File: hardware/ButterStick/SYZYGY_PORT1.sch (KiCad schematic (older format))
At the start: 2 parts, among them U3 ECP5U25

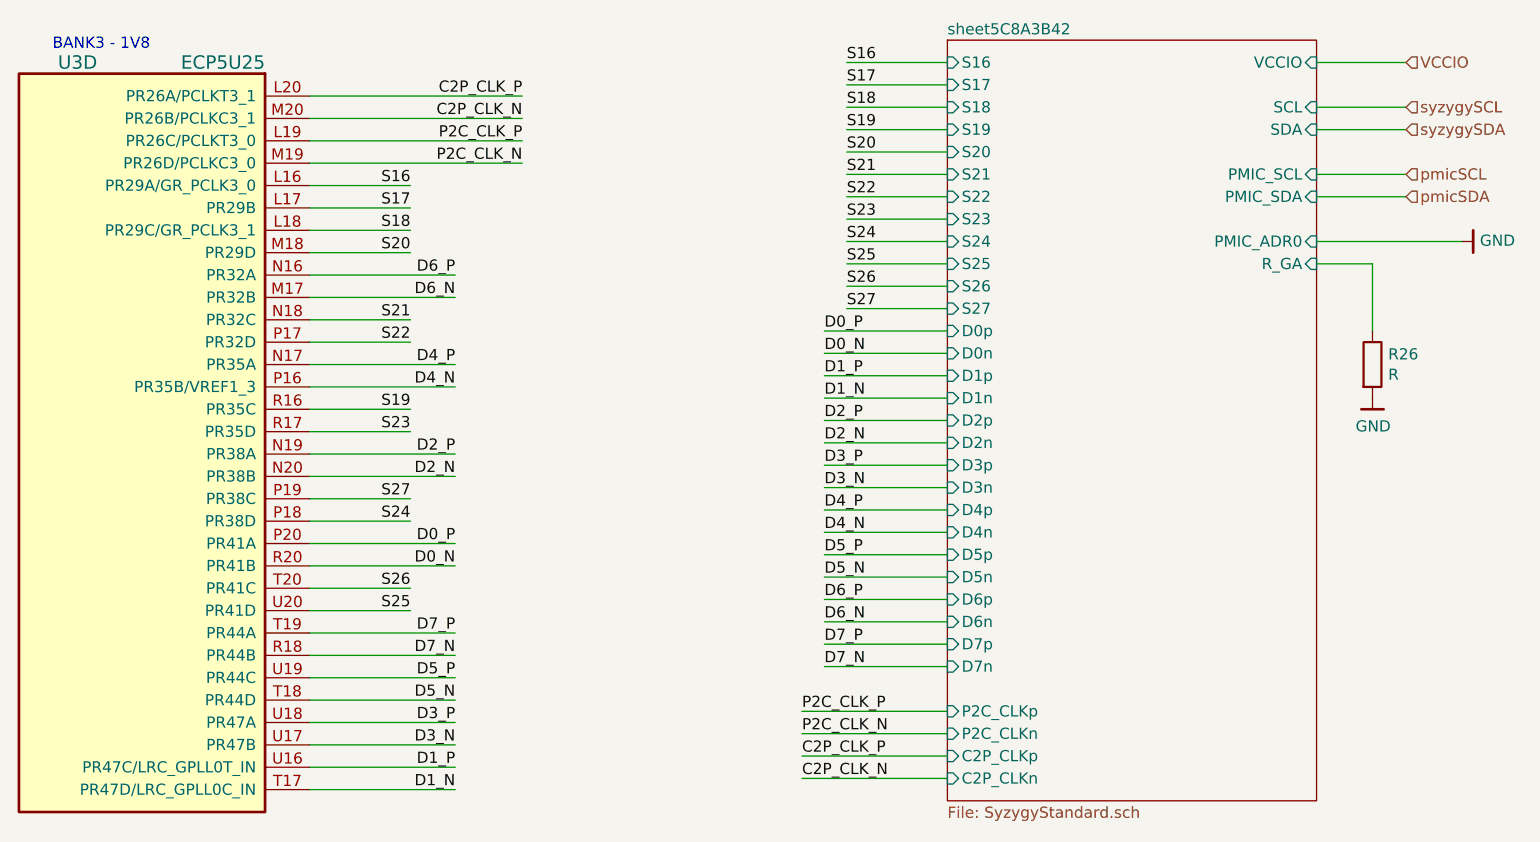
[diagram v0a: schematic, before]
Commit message: Routed all SYZYGY ports. Placed decoupling caps etc.
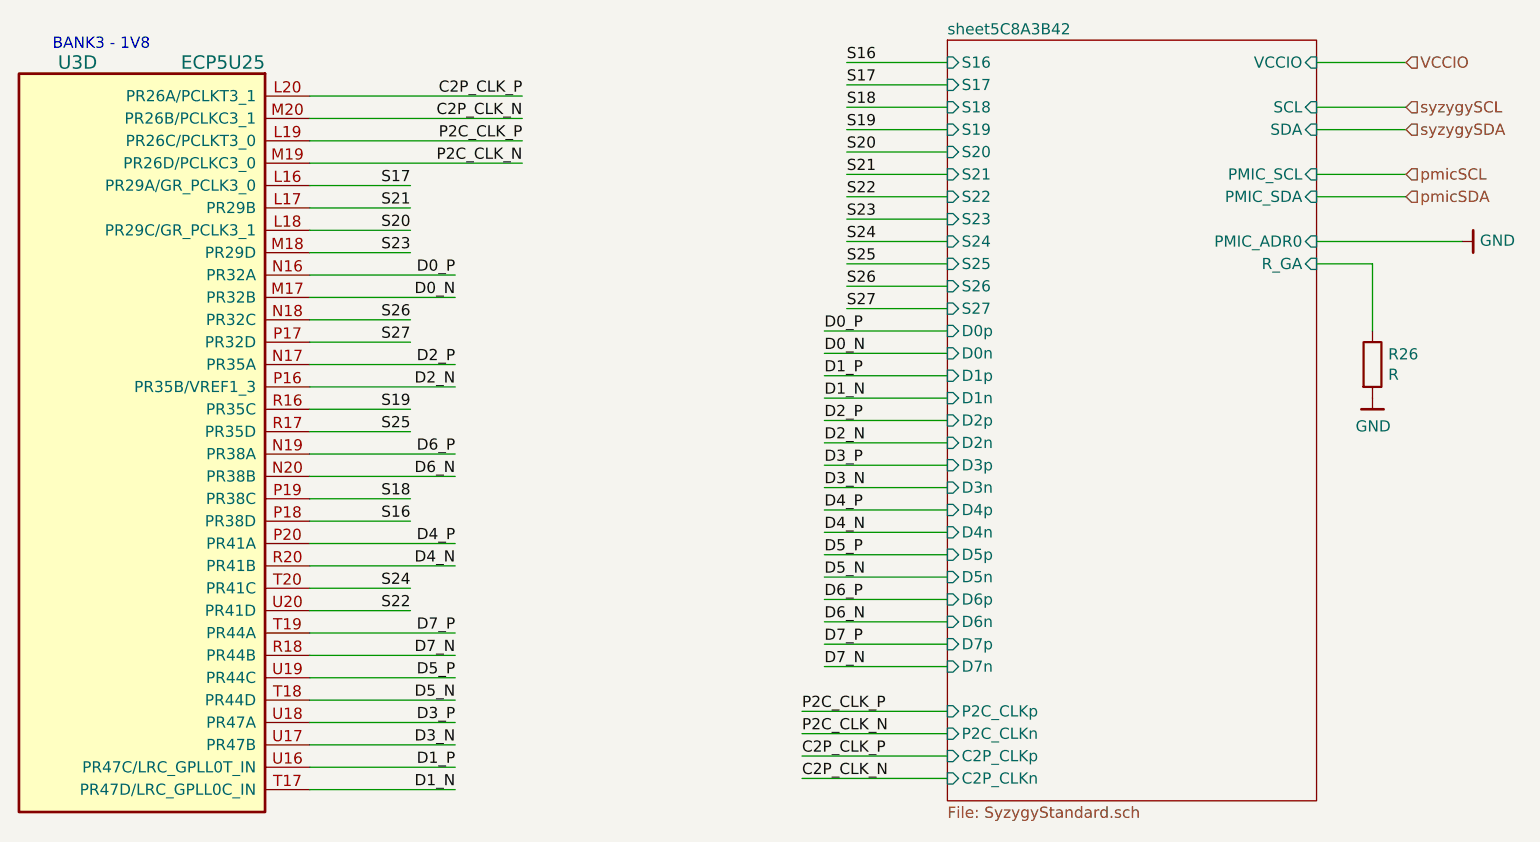
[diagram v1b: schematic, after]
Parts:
- R26: footprint (none) -> pkl_dipol:R_0402
- U3: footprint (none) -> gkl_housings_bga:caBGA_381_17x17
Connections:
- net D0_N: now also U3.M17 (PR32B); no longer U3.R20 (PR41B)
- net D0_P: now also U3.N16 (PR32A); no longer U3.P20 (PR41A)
- net D2_N: now also U3.P16 (PR35B/VREF1_3); no longer U3.N20 (PR38B)
- net D2_P: now also U3.N17 (PR35A); no longer U3.N19 (PR38A)
- net D4_N: now also U3.R20 (PR41B); no longer U3.P16 (PR35B/VREF1_3)
- net D4_P: now also U3.P20 (PR41A); no longer U3.N17 (PR35A)
- net D6_N: now also U3.N20 (PR38B); no longer U3.M17 (PR32B)
- net D6_P: now also U3.N19 (PR38A); no longer U3.N16 (PR32A)
- net S16: now also U3.P18 (PR38D); no longer U3.L16 (PR29A/GR_PCLK3_0)
- net S17: now also U3.L16 (PR29A/GR_PCLK3_0); no longer U3.L17 (PR29B)
- net S18: now also U3.P19 (PR38C); no longer U3.L18 (PR29C/GR_PCLK3_1)
- net S20: now also U3.L18 (PR29C/GR_PCLK3_1); no longer U3.M18 (PR29D)
- net S21: now also U3.L17 (PR29B); no longer U3.N18 (PR32C)
- net S22: now also U3.U20 (PR41D); no longer U3.P17 (PR32D)
- net S23: now also U3.M18 (PR29D); no longer U3.R17 (PR35D)
- net S24: now also U3.T20 (PR41C); no longer U3.P18 (PR38D)
- net S25: now also U3.R17 (PR35D); no longer U3.U20 (PR41D)
- net S26: now also U3.N18 (PR32C); no longer U3.T20 (PR41C)
- net S27: now also U3.P17 (PR32D); no longer U3.P19 (PR38C)
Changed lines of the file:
@@
 $Descr A4 11693 8268
 encoding utf-8
-Sheet 10 13
+Sheet 10 14
 Title ""
 Date ""
@@
 F 0 "U3" H 4600 2600 60  0000 L CNN
 F 1 "ECP5U25" H 3850 2600 60  0000 L CNN
-F 2 "" H 3650 2450 50  0001 C CNN
+F 2 "gkl_housings_bga:caBGA_381_17x17" H 3650 2450 50  0001 C CNN
 F 3 "" H 3650 2450 50  0001 C CNN
 F 4 " 220-2052-ND " H -200 -1950 50  0001 C CNN "SN-DK"
@@
 C2P_CLK_N
 Wire Wire Line
+	3650 4350 4100 4350
+Wire Wire Line
 	3650 2850 4100 2850
 Wire Wire Line
+	3650 4250 4100 4250
+Wire Wire Line
+	3650 3850 4100 3850
+Wire Wire Line
+	3650 3050 4100 3050
+Wire Wire Line
 	3650 2950 4100 2950
 Wire Wire Line
-	3650 3050 4100 3050
-Wire Wire Line
-	3650 3850 4100 3850
+	3650 4750 4100 4750
 Wire Wire Line
 	3650 3150 4100 3150
 Wire Wire Line
+	3650 4650 4100 4650
+Wire Wire Line
+	3650 3950 4100 3950
+Wire Wire Line
 	3650 3450 4100 3450
 Wire Wire Line
 	3650 3550 4100 3550
 Wire Wire Line
-	3650 3950 4100 3950
-Wire Wire Line
-	3650 4350 4100 4350
-Wire Wire Line
-	3650 4750 4100 4750
-Wire Wire Line
-	3650 4650 4100 4650
-Wire Wire Line
-	3650 4250 4100 4250
+	3650 3250 4300 3250
+Wire Wire Line
+	3650 3350 4300 3350
+Wire Wire Line
+	3650 5450 4300 5450
+Wire Wire Line
+	3650 5550 4300 5550
+Wire Wire Line
+	3650 3650 4300 3650
+Wire Wire Line
+	3650 3750 4300 3750
+Wire Wire Line
+	3650 5250 4300 5250
+Wire Wire Line
+	3650 5350 4300 5350
 Wire Wire Line
 	3650 4450 4300 4450
@@
 	3650 4550 4300 4550
 Wire Wire Line
-	3650 5450 4300 5450
-Wire Wire Line
-	3650 5550 4300 5550
+	3650 5050 4300 5050
+Wire Wire Line
+	3650 5150 4300 5150
 Wire Wire Line
 	3650 4050 4300 4050
@@
 	3650 4150 4300 4150
 Wire Wire Line
-	3650 5250 4300 5250
-Wire Wire Line
-	3650 5350 4300 5350
-Wire Wire Line
-	3650 3650 4300 3650
-Wire Wire Line
-	3650 3750 4300 3750
-Wire Wire Line
-	3650 5050 4300 5050
-Wire Wire Line
-	3650 5150 4300 5150
-Wire Wire Line
-	3650 3250 4300 3250
-Wire Wire Line
-	3650 3350 4300 3350
-Wire Wire Line
 	3650 4850 4300 4850
 Wire Wire Line
@@
 Wire Wire Line
 	3650 2550 4600 2550
+Text Label 4100 4350 2    50   ~ 0
+S16
 Text Label 4100 2850 2    50   ~ 0
-S16
-Text Label 4100 2950 2    50   ~ 0
 S17
-Text Label 4100 3050 2    50   ~ 0
+Text Label 4100 4250 2    50   ~ 0
 S18
 Text Label 4100 3850 2    50   ~ 0
 S19
+Text Label 4100 3050 2    50   ~ 0
+S20
+Text Label 4100 2950 2    50   ~ 0
+S21
+Text Label 4100 4750 2    50   ~ 0
+S22
 Text Label 4100 3150 2    50   ~ 0
-S20
+S23
+Text Label 4100 4650 2    50   ~ 0
+S24
+Text Label 4100 3950 2    50   ~ 0
+S25
 Text Label 4100 3450 2    50   ~ 0
-S21
+S26
 Text Label 4100 3550 2    50   ~ 0
-S22
-Text Label 4100 3950 2    50   ~ 0
-S23
-Text Label 4100 4350 2    50   ~ 0
-S24
-Text Label 4100 4750 2    50   ~ 0
-S25
-Text Label 4100 4650 2    50   ~ 0
-S26
-Text Label 4100 4250 2    50   ~ 0
 S27
-Text Label 4300 4450 2    50   ~ 0
+Text Label 4300 3250 2    50   ~ 0
 D0_P
-Text Label 4300 4550 2    50   ~ 0
+Text Label 4300 3350 2    50   ~ 0
 D0_N
 Text Label 4300 5450 2    50   ~ 0
@@
 Text Label 4300 5550 2    50   ~ 0
 D1_N
-Text Label 4300 4050 2    50   ~ 0
+Text Label 4300 3650 2    50   ~ 0
 D2_P
-Text Label 4300 4150 2    50   ~ 0
+Text Label 4300 3750 2    50   ~ 0
 D2_N
 Text Label 4300 5250 2    50   ~ 0
@@
 Text Label 4300 5350 2    50   ~ 0
 D3_N
-Text Label 4300 3650 2    50   ~ 0
+Text Label 4300 4450 2    50   ~ 0
 D4_P
-Text Label 4300 3750 2    50   ~ 0
+Text Label 4300 4550 2    50   ~ 0
 D4_N
 Text Label 4300 5050 2    50   ~ 0
@@
 Text Label 4300 5150 2    50   ~ 0
 D5_N
-Text Label 4300 3250 2    50   ~ 0
+Text Label 4300 4050 2    50   ~ 0
 D6_P
-Text Label 4300 3350 2    50   ~ 0
+Text Label 4300 4150 2    50   ~ 0
 D6_N
 Text Label 4300 4850 2    50   ~ 0
@@
 F 0 "R26" H 8470 3696 50  0000 L CNN
 F 1 "R" H 8470 3605 50  0000 L CNN
-F 2 "" V 8330 3650 50  0001 C CNN
+F 2 "pkl_dipol:R_0402" V 8330 3650 50  0001 C CNN
 F 3 "~" H 8400 3650 50  0001 C CNN
 	1    8400 3650

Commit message: Finished initial routing of PCB.. Most parts are finished.
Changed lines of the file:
@@
 $Descr A4 11693 8268
 encoding utf-8
-Sheet 10 13
+Sheet 9 13
 Title ""
 Date ""
@@
 F39 "VCCIO" I R 8150 2300 50
 F40 "R_GA" I R 8150 3200 50
+F41 "PMIC_EN" I R 8150 2400 50
 $EndSheet
 Wire Wire Line
@@
 Text HLabel 8550 2900 2    50   Input ~ 0
 pmicSDA
+Wire Wire Line
+	8150 2400 8550 2400
+Text HLabel 8550 2400 2    50   Input ~ 0
+EN
 $EndSCHEMATC

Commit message: Update KiCad PCB.
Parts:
- U3: PN LFE5U-25F-6BG381I -> LFE5U-45F-8BG381C
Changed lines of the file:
@@
 F 3 "" H 3650 2450 50  0001 C CNN
 F 4 " 220-2052-ND " H -200 -1950 50  0001 C CNN "SN-DK"
-F 5 " LFE5U-25F-6BG381I " H -200 -1950 50  0001 C CNN "PN"
+F 5 "LFE5U-45F-8BG381C" H -200 -1950 50  0001 C CNN "PN"
 F 6 "Lattice" H -200 -1950 50  0001 C CNN "Mfg"
 	4    3650 2450

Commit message: Finalised part values update BOM values to reflect. Swapped layers 4/5 due to stackup changes
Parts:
- R26: value R -> 84k5; Mfg (none) -> Stackpole Electronics Inc; PN (none) -> RMCF0402FT84K5; Tol (none) -> 1%
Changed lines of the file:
@@
 EESchema Schematic File Version 4
 LIBS:ButterStick-cache
-EELAYER 26 0
+EELAYER 29 0
 EELAYER END
 $Descr A4 11693 8268
 encoding utf-8
-Sheet 9 13
-Title ""
-Date ""
-Rev ""
-Comp ""
+Sheet 7 13
+Title "ButterStick"
+Date "2019-03-19"
+Rev "r0_1"
+Comp "GsD"
 Comment1 ""
 Comment2 ""
@@
 AR Path="/5C80F19D/5C996E36" Ref="R26"  Part="1"
 F 0 "R26" H 8470 3696 50  0000 L CNN
-F 1 "R" H 8470 3605 50  0000 L CNN
+F 1 "84k5" H 8470 3605 50  0000 L CNN
 F 2 "pkl_dipol:R_0402" V 8330 3650 50  0001 C CNN
 F 3 "~" H 8400 3650 50  0001 C CNN
+F 4 "Stackpole Electronics Inc" H 0   0   50  0001 C CNN "Mfg"
+F 5 "RMCF0402FT84K5" H 0   0   50  0001 C CNN "PN"
+F 6 "1%" H 0   0   50  0001 C CNN "Tol"
 	1    8400 3650
 	1    0    0    -1
